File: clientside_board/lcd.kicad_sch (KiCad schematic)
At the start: 2 parts, among them J12 Conn_02x09_Odd_Even, J9 Potentiometer Connector

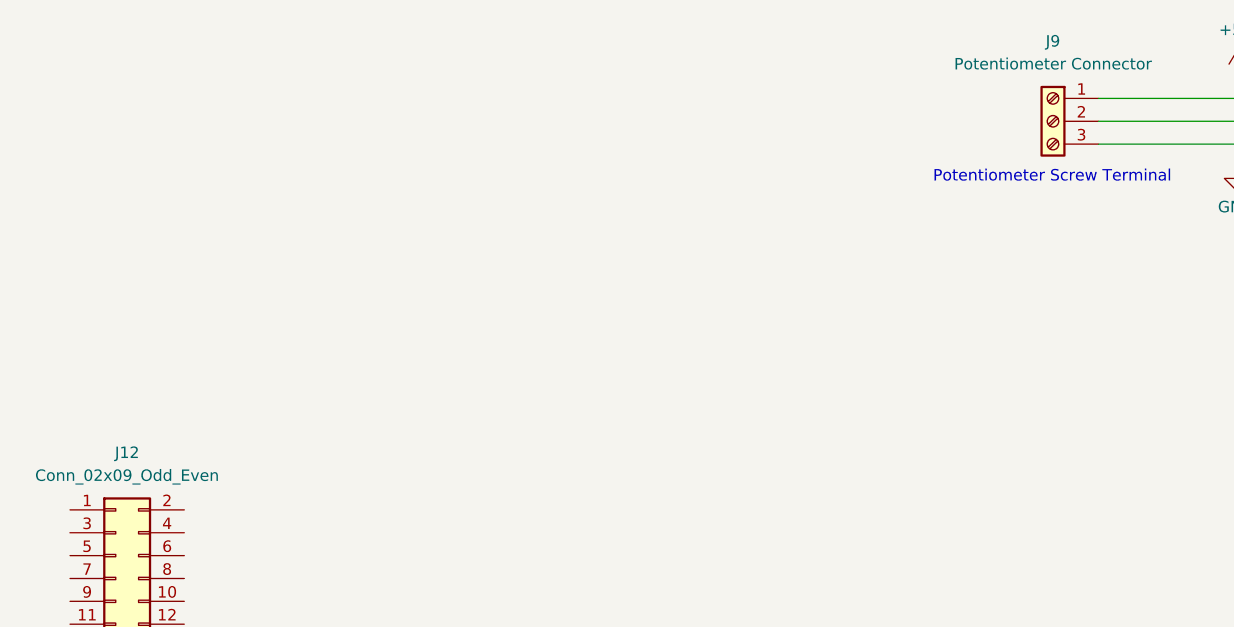
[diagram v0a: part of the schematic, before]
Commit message: Cleanup Power and Ethernet Sheet
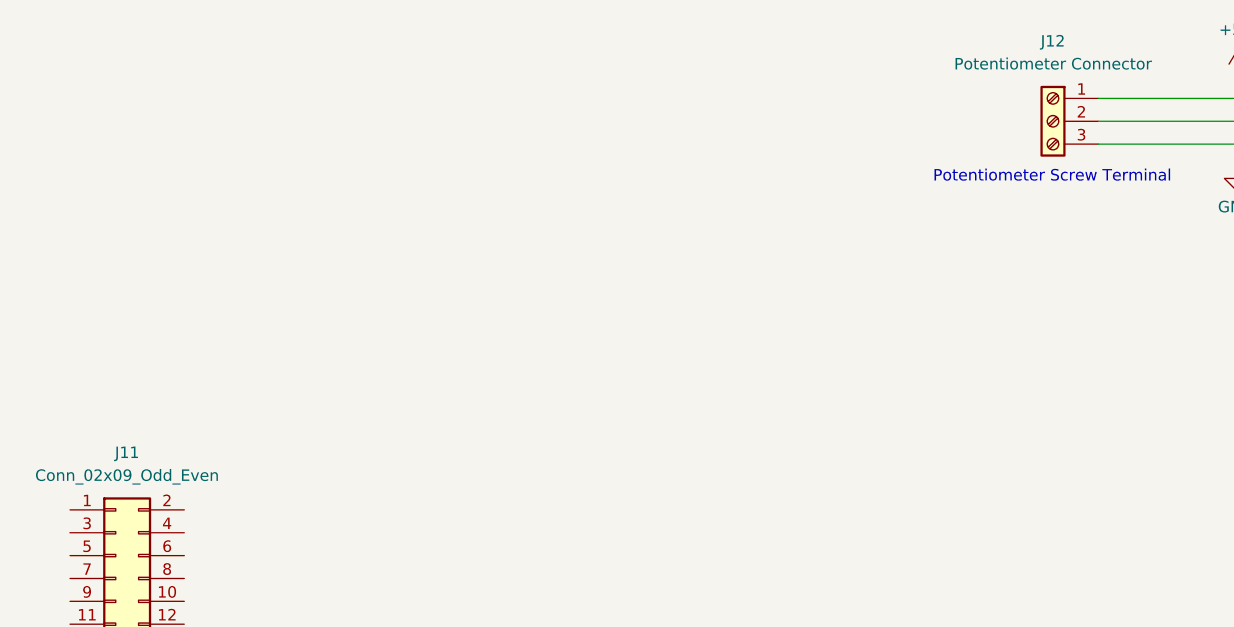
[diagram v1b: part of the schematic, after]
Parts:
- renumbered J12 to J11, J9 to J12
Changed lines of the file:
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@@
 		(dnp no)
 		(fields_autoplaced yes)
-		(property "Reference" "#PWR060"
+		(property "Reference" "#PWR077"
 			(at 250.19 50.8 0)
 			(effects
@@
 			(project "clientside_board"
 				(path "/94506b77-3097-414f-927c-35c0af27646f/023e7328-87f3-46e3-af02-c5d7acdf81d2"
-					(reference "#PWR060")
+					(reference "#PWR077")
 					(unit 1)
 				)
@@
 		(dnp no)
 		(fields_autoplaced yes)
-		(property "Reference" "#PWR059"
+		(property "Reference" "#PWR076"
 			(at 250.19 38.1 0)
 			(effects
@@
 			(project "clientside_board"
 				(path "/94506b77-3097-414f-927c-35c0af27646f/023e7328-87f3-46e3-af02-c5d7acdf81d2"
-					(reference "#PWR059")
+					(reference "#PWR076")
 					(unit 1)
 				)
@@
 		(dnp no)
 		(fields_autoplaced yes)
-		(property "Reference" "J9"
+		(property "Reference" "J12"
 			(at 229.87 30.48 0)
 			(effects
@@
 			(project "clientside_board"
 				(path "/94506b77-3097-414f-927c-35c0af27646f/023e7328-87f3-46e3-af02-c5d7acdf81d2"
-					(reference "J9")
+					(reference "J12")
 					(unit 1)
 				)
@@
 		(dnp no)
 		(fields_autoplaced yes)
-		(property "Reference" "J12"
+		(property "Reference" "J11"
 			(at 127 76.2 0)
 			(effects
@@
 			(project ""
 				(path "/94506b77-3097-414f-927c-35c0af27646f/023e7328-87f3-46e3-af02-c5d7acdf81d2"
-					(reference "J12")
-					(unit 1)
-				)
+					(reference "J11")
+					(unit 1)
+				)

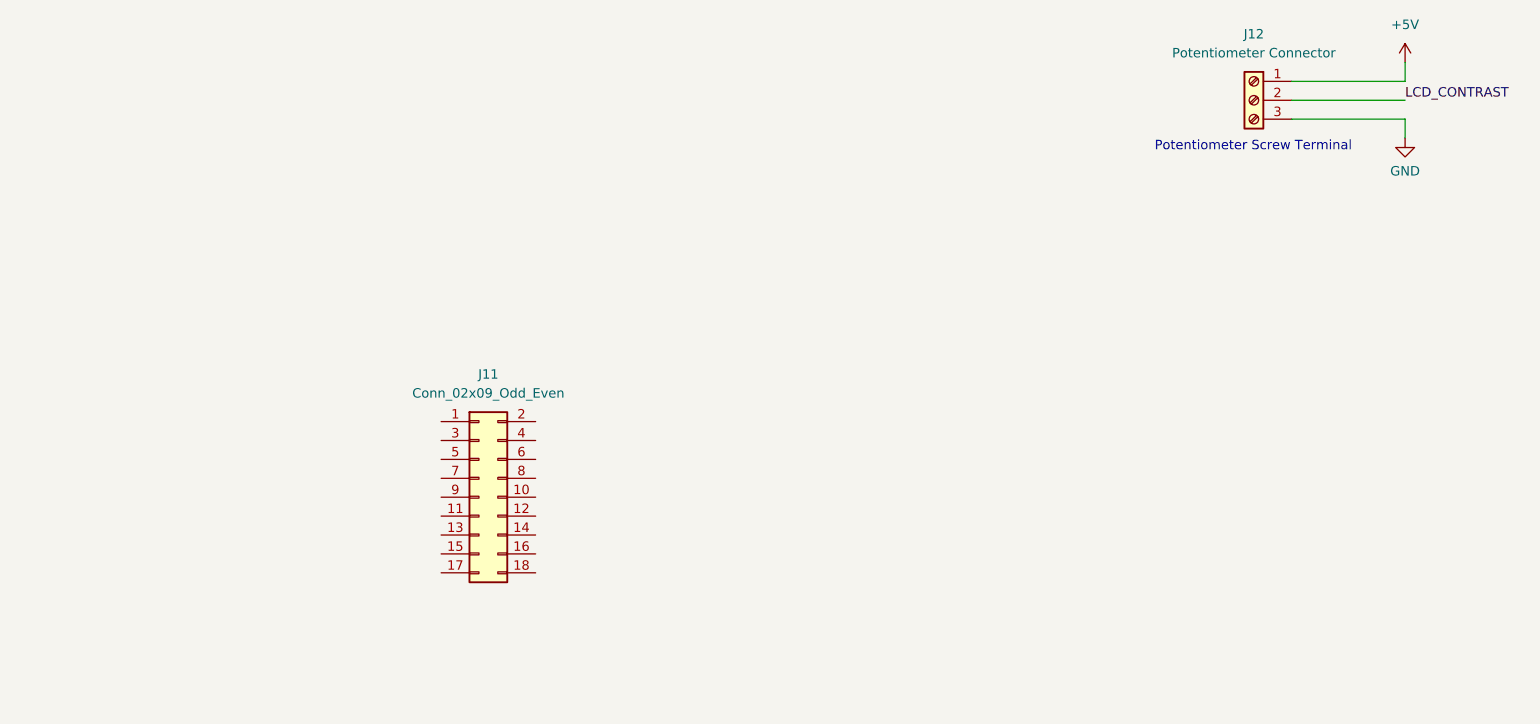
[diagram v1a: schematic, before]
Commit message: Start MCU pin connection
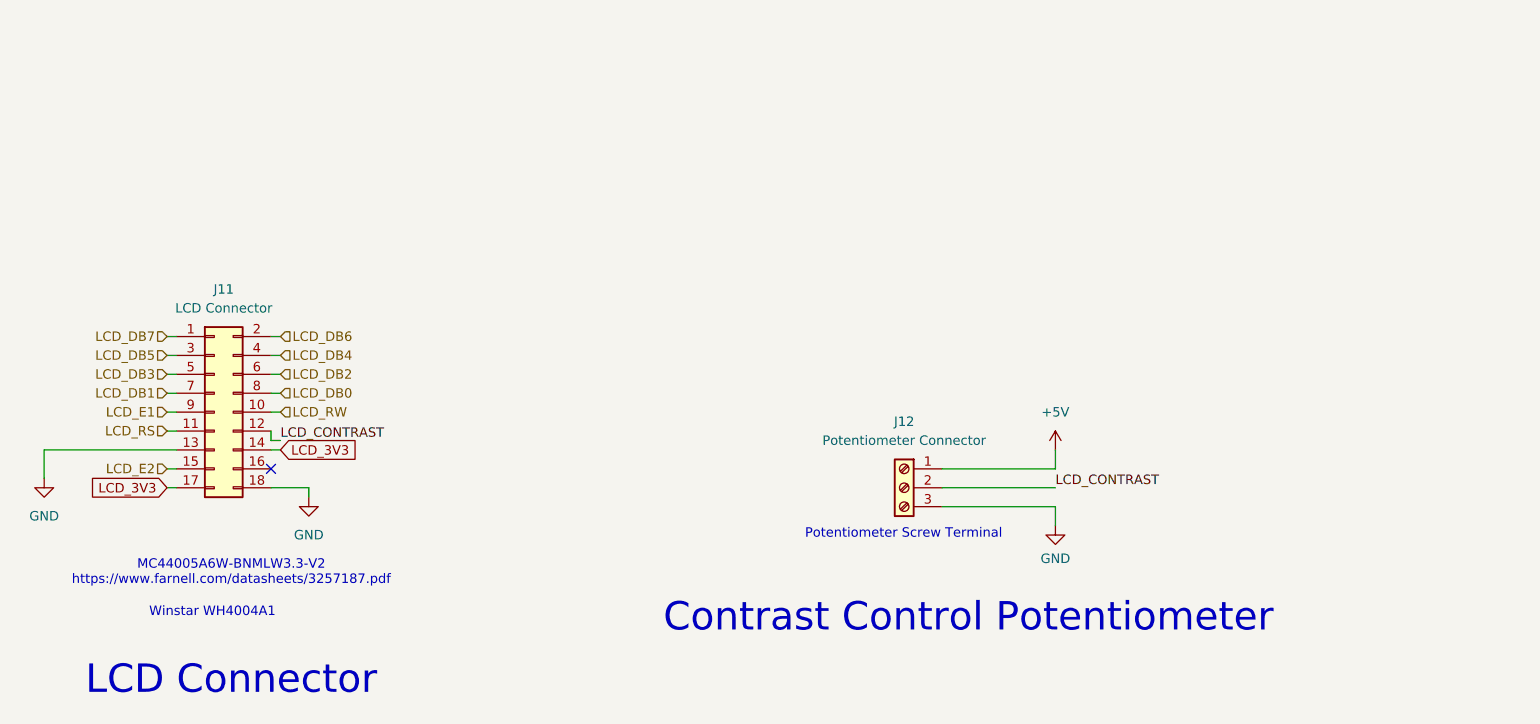
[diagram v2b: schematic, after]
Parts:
- J11: value Conn_02x09_Odd_Even -> LCD Connector
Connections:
- net GND: now also J11.13 (Pin_13), J11.18 (Pin_18)
- net LCD_CONTRAST: now also J11.12 (Pin_12)
- net LCD_DB7: now reaches J11.1 (Pin_1)
- net LCD_RW: now reaches J11.10 (Pin_10)
- net LCD_RS: now reaches J11.11 (Pin_11)
- net LCD_3V3: now reaches J11.14 (Pin_14)
- net LCD_3V3: now also J11.17 (Pin_17)
- net LCD_E2: now reaches J11.15 (Pin_15)
- net LCD_DB6: now reaches J11.2 (Pin_2)
- net LCD_DB5: now reaches J11.3 (Pin_3)
- net LCD_DB4: now reaches J11.4 (Pin_4)
- net LCD_DB3: now reaches J11.5 (Pin_5)
- net LCD_DB2: now reaches J11.6 (Pin_6)
- net LCD_DB1: now reaches J11.7 (Pin_7)
- net LCD_DB0: now reaches J11.8 (Pin_8)
- net LCD_E1: now reaches J11.9 (Pin_9)
- no-connect marks 0 -> 1
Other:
- note added: "Contrast Control Potentiometer"
- note added: "LCD Connector"
- note added: "MC44005A6W-BNMLW3.3-V2 https://www.farnell.com/datasheets/3257187.pdf"
- note added: "Winstar WH4004A1"
- moved on the sheet: J11, J12

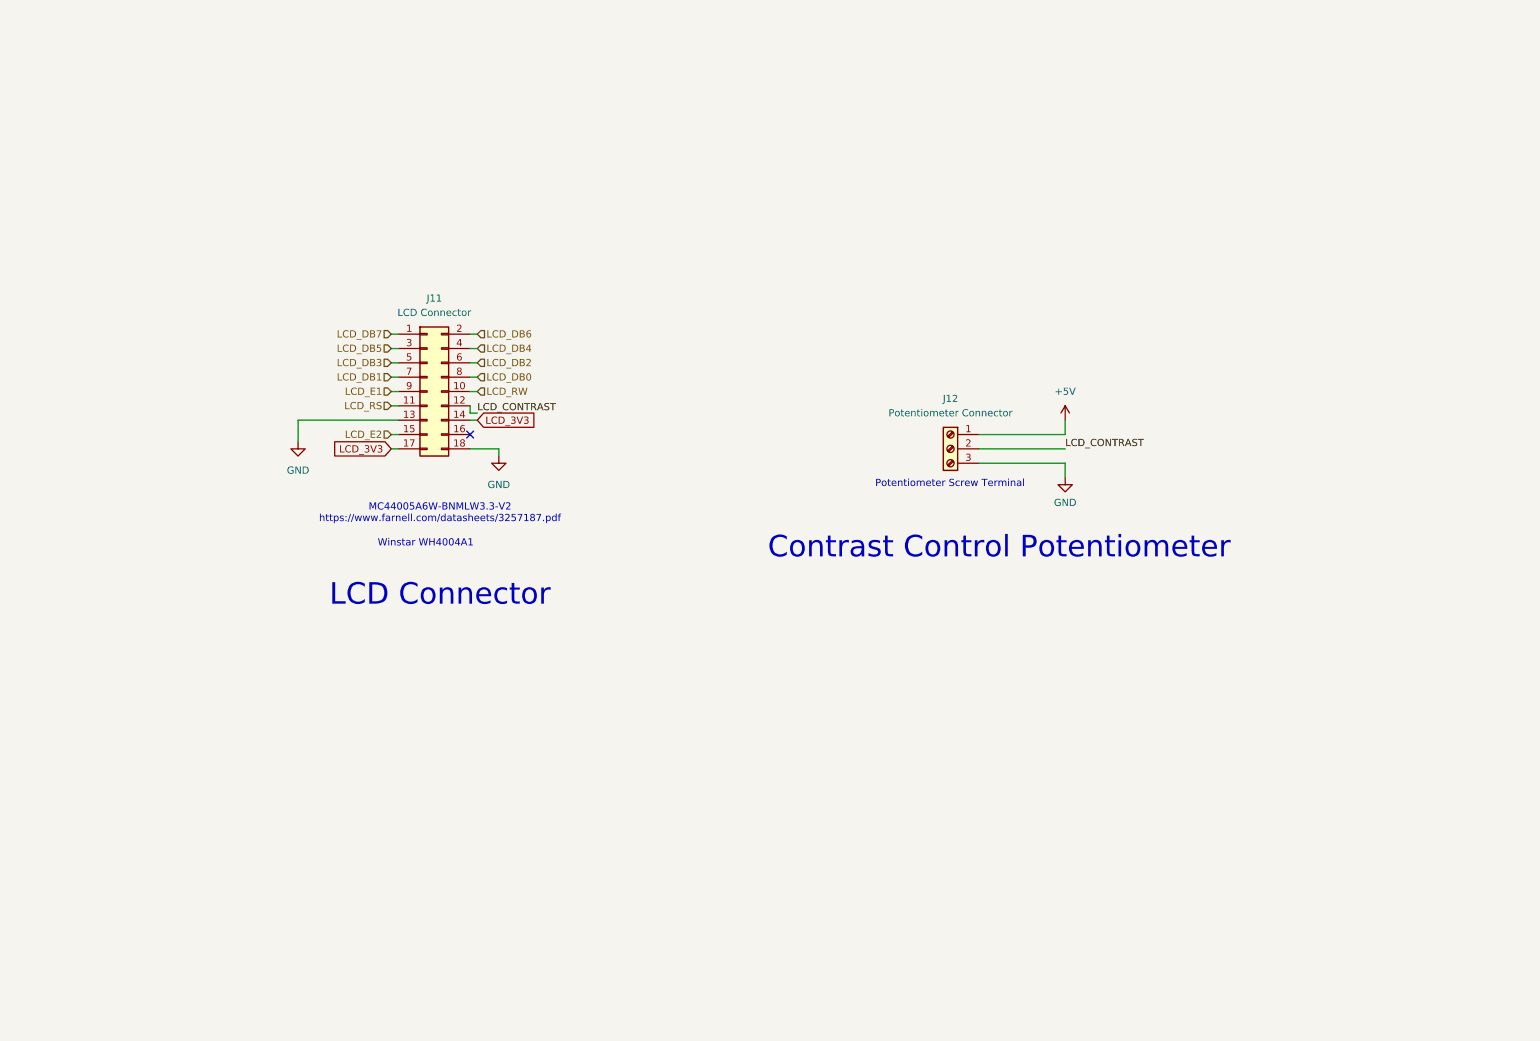
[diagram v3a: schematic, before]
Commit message: Integrate new LCD display module
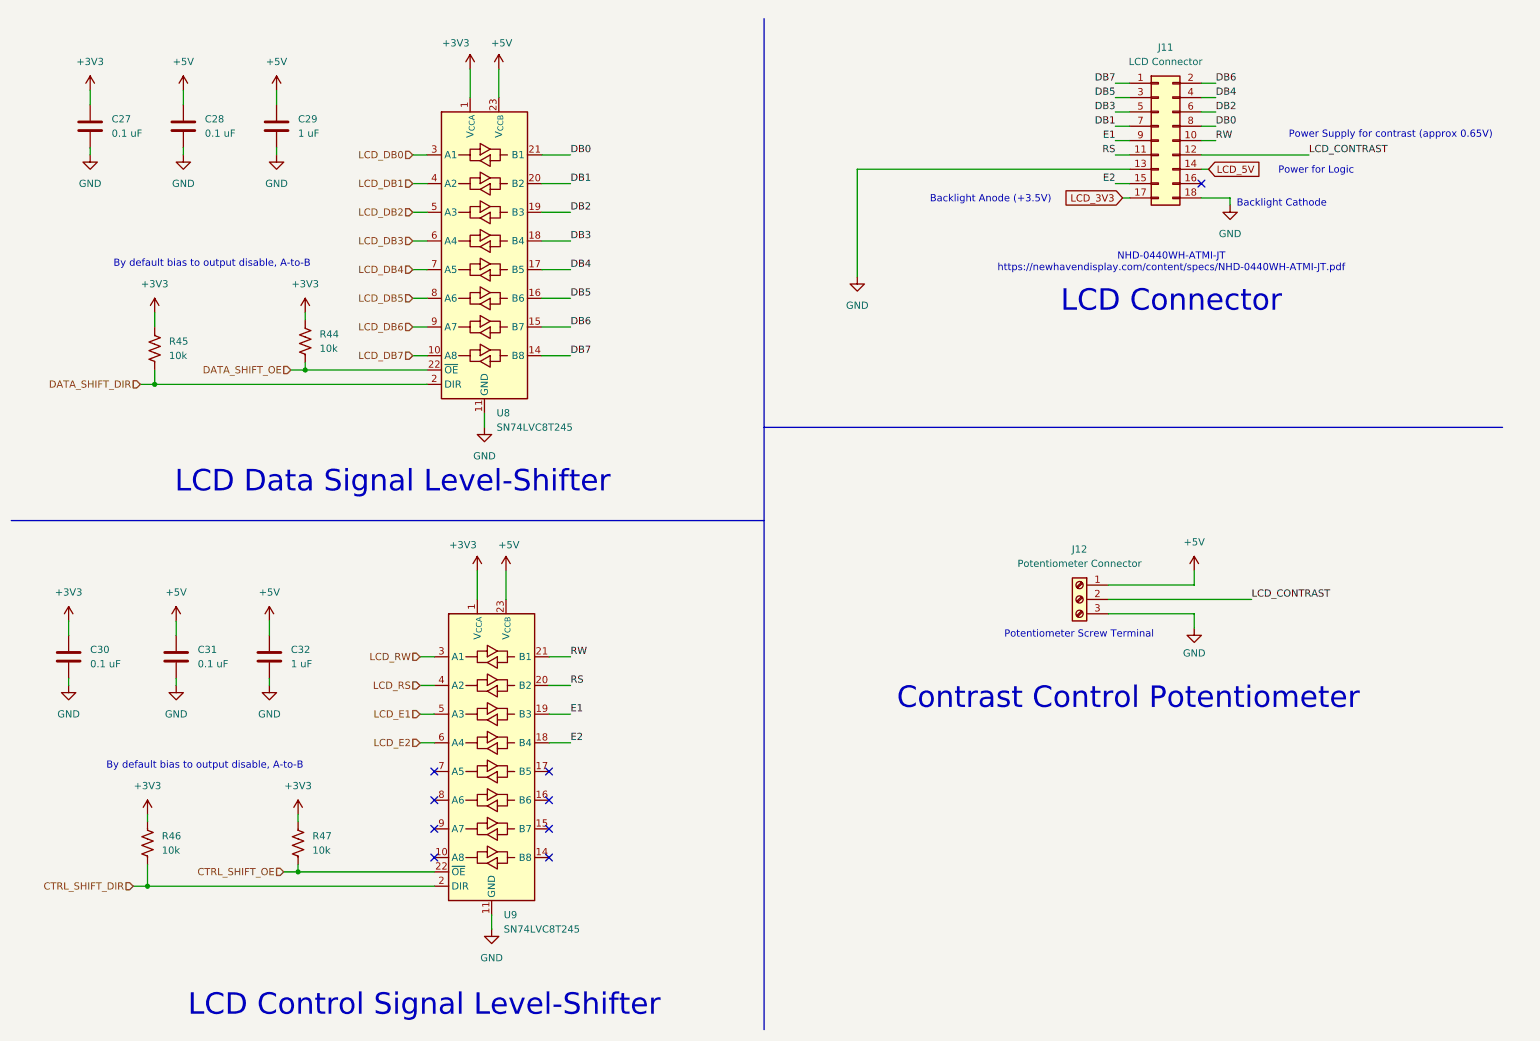
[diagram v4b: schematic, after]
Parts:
- added C27, C28, C30, C31: 0.1 uF, symbol Device:C
- added C29, C32: 1 uF, symbol Device:C
- added R44, R45, R46, R47: 10k, symbol Device:R_US
- added U8, U9: SN74LVC8T245, symbol Logic_LevelTranslator:SN74LVC8T245
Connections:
- net +5V: now also C28.1, C29.1, C31.1, C32.1, U8.23 (V_{CCB}), U8.24 (V_{CCB}), U9.23 (V_{CCB}), U9.24 (V_{CCB})
- net GND: now also C27.2, C28.2, C29.2, C30.2, C31.2, C32.2, U8.11 (GND), U8.12 (GND), U8.13 (GND), U9.11 (GND), U9.12 (GND), U9.13 (GND)
- net LCD_3V3: no longer J11.14 (Pin_14)
- net LCD_DB0: now also U8.3 (A1); no longer J11.8 (Pin_8)
- net LCD_DB1: now also U8.4 (A2); no longer J11.7 (Pin_7)
- net LCD_DB2: now also U8.5 (A3); no longer J11.6 (Pin_6)
- net LCD_DB3: now also U8.6 (A4); no longer J11.5 (Pin_5)
- net LCD_DB4: now also U8.7 (A5); no longer J11.4 (Pin_4)
- net LCD_DB5: now also U8.8 (A6); no longer J11.3 (Pin_3)
- net LCD_DB6: now also U8.9 (A7); no longer J11.2 (Pin_2)
- net LCD_DB7: now also U8.10 (A8); no longer J11.1 (Pin_1)
- net LCD_E1: now also U9.5 (A3); no longer J11.9 (Pin_9)
- net LCD_E2: now also U9.6 (A4); no longer J11.15 (Pin_15)
- net LCD_RS: now also U9.4 (A2); no longer J11.11 (Pin_11)
- net LCD_RW: now also U9.3 (A1); no longer J11.10 (Pin_10)
- new net +3V3: C27.1, C30.1, R44.1, R45.1, R46.1, R47.1, U8.1 (V_{CCA}), U9.1 (V_{CCA})
- new net CTRL_SHIFT_DIR: R46.2, U9.2 (DIR)
- new net CTRL_SHIFT_OE: R47.2, U9.22 (~{OE})
- new net DATA_SHIFT_DIR: R45.2, U8.2 (DIR)
- new net DATA_SHIFT_OE: R44.2, U8.22 (~{OE})
- new net DB0: J11.8 (Pin_8), U8.21 (B1)
- new net DB1: J11.7 (Pin_7), U8.20 (B2)
- new net DB2: J11.6 (Pin_6), U8.19 (B3)
- new net DB3: J11.5 (Pin_5), U8.18 (B4)
- new net DB4: J11.4 (Pin_4), U8.17 (B5)
- new net DB5: J11.3 (Pin_3), U8.16 (B6)
- new net DB6: J11.2 (Pin_2), U8.15 (B7)
- new net DB7: J11.1 (Pin_1), U8.14 (B8)
- new net E1: J11.9 (Pin_9), U9.19 (B3)
- new net E2: J11.15 (Pin_15), U9.18 (B4)
- new net LCD_5V: J11.14 (Pin_14)
- new net RS: J11.11 (Pin_11), U9.20 (B2)
- new net RW: J11.10 (Pin_10), U9.21 (B1)
- no-connect marks 1 -> 9
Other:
- note added: "Backlight Anode (+3.5V)"
- note added: "Backlight Cathode"
- note added: "By default bias to output disable, A-to-B"
- note added: "LCD Control Signal Level-Shifter"
- note added: "LCD Data Signal Level-Shifter"
- note added: "NHD-0440WH-ATMI-JT https://newhavendisplay.com/content/specs/NHD-0440WH-ATMI-JT.pdf"
- note added: "Power Supply for contrast (approx 0.65V)"
- note added: "Power for Logic"
- note removed: "MC44005A6W-BNMLW3.3-V2 https://www.farnell.com/datasheets/3257187.pdf"
- note removed: "Winstar WH4004A1"
- moved on the sheet: J11, J12
